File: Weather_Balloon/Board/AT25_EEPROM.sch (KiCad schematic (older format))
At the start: 20 parts, among them U10 AT25_EEPROM, U11 AT25_EEPROM, U12 AT25_EEPROM, U13 AT25_EEPROM, U14 AT25_EEPROM, U15 AT25_EEPROM, U6 AT25_EEPROM, U7 AT25_EEPROM, U8 AT25_EEPROM, U9 AT25_EEPROM

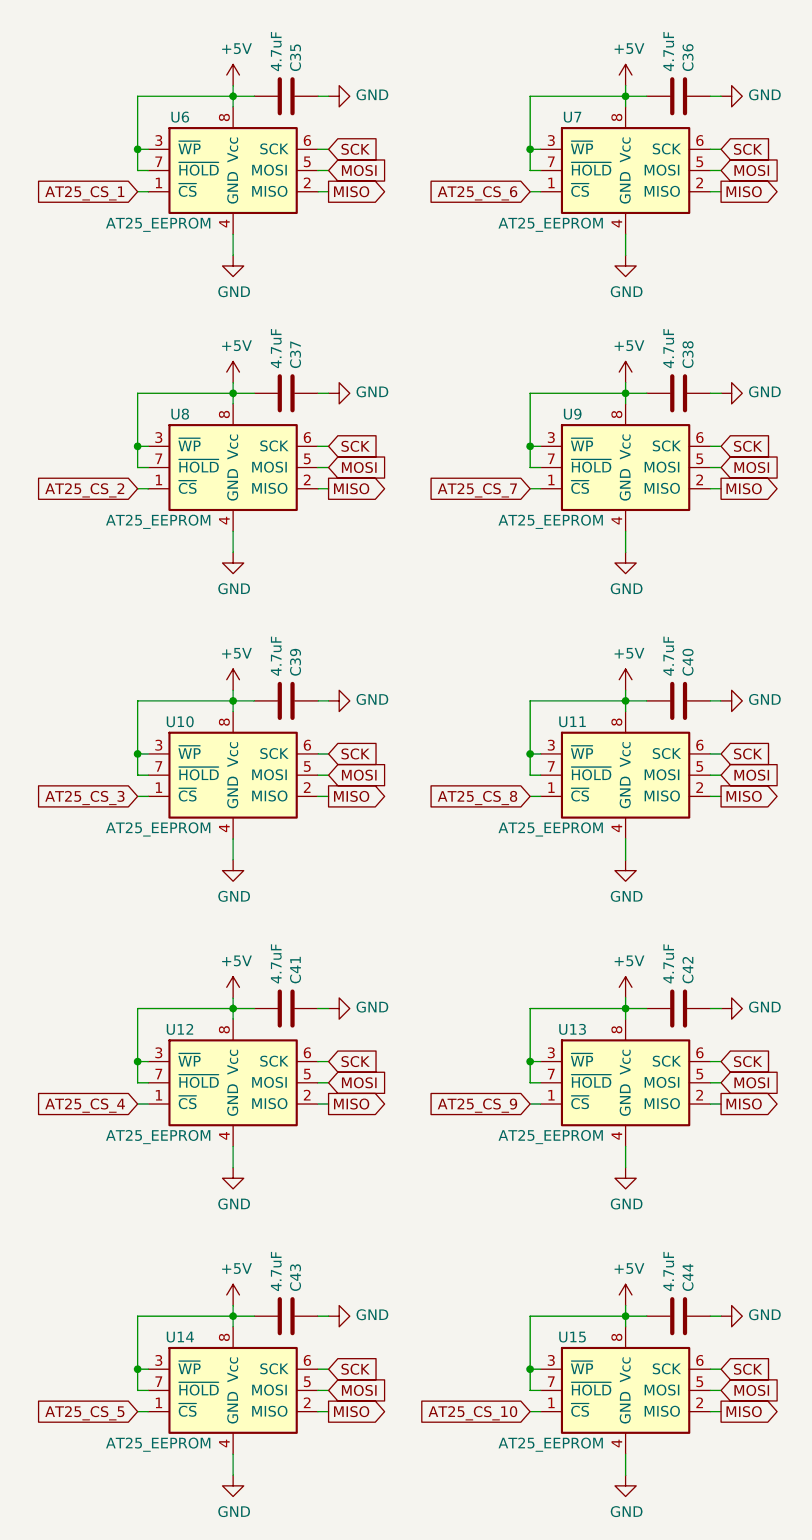
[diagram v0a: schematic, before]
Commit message: Updated PCB board for larger traces and more compact design.
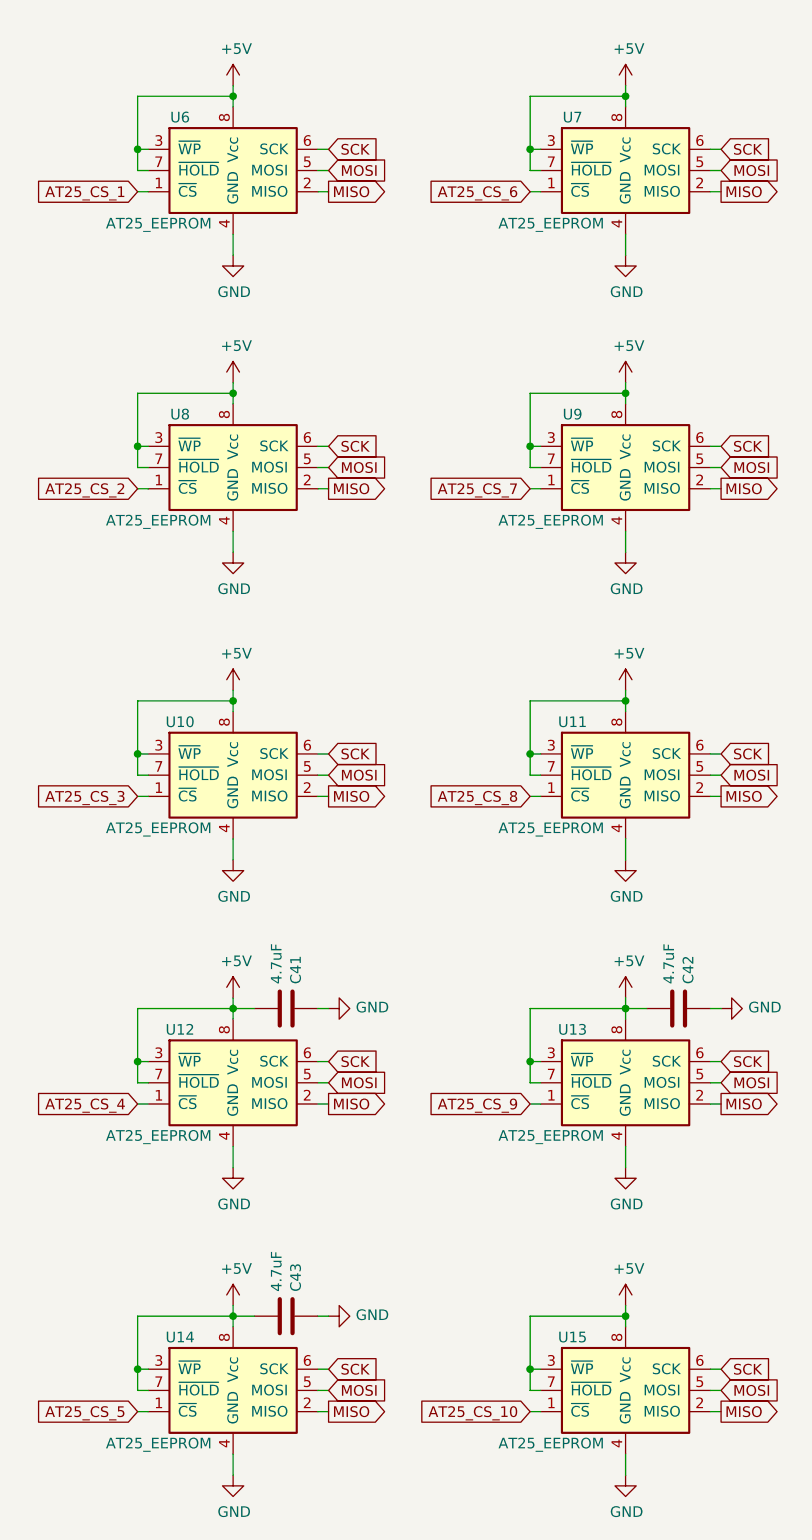
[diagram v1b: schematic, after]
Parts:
- removed C35, C36, C37, C38, C39, C40, C44: 4.7uF, Capacitors_SMD:C_0603_HandSoldering, symbol C
